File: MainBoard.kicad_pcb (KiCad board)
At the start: 2 copper layers, 95 x 140 mm, 86 parts, among them J1 Conn_01x04, J10 Conn_01x02, J11 Conn_01x03, J12 Conn_01x03, J13 Conn_01x04, J14 Conn_01x03, J15 Conn_01x04, J16 Conn_01x05, J17 Conn_01x05, J18 Conn_01x06, J19 Conn_01x05, J2 Conn_01x04, J20 Conn_01x08, J21 Conn_01x03, J22 Conn_01x03, J23 Conn_01x05, J24 Conn_01x04, J25 Conn_01x04, J26 Conn_01x04, J27 Conn_01x04, J28 Conn_01x04, J3 Conn_01x06, J4 Conn_01x02, J5 Conn_01x02, J6 Conn_01x02, J7 Conn_01x04, J8 Conn_01x04, J9 Conn_01x02, Q1 NMOS_80A, Q10 NMOS_80A, Q11 NMOS_80A, Q2 NMOS_80A, Q3 NMOS_80A, Q4 NMOS, Q5 NMOS, Q6 NMOS, Q7 NMOS, Q8 NMOS, Q9 NMOS, U1 TJA1051T-3, U10 INA228, U2 INA228, U5 INA228, U6 ESP32-DEVKITC-32D, U7 MCP23017_SO, U8 MCP23017_SO, U9 INA228

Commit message: routed a few more track
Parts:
- moved J20 0.79 mm to (100.0, 62.8)
- moved J25 0.49 mm to (108.8, 71.0)
- moved J26 0.24 mm to (109.0, 84.0)
- moved J27 0.24 mm to (109.0, 97.0)
- moved J28 0.16 mm to (109.0, 110.0)
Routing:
- net BRAKE_LEFT_INPUT: track 0.00 -> 132.3 mm, vias 0 -> 3
- net Net-(D6-DOUT): track 0.00 -> 106.3 mm, vias 0 -> 2
- net MAP_INPUT: track 0.00 -> 70.7 mm, vias 0 -> 2
- net MAP_LED: track 0.00 -> 61.6 mm, vias 0 -> 2
- net SDA: track 0.00 -> 44.5 mm, vias 0 -> 2
- net SCL: track 0.00 -> 43.0 mm, vias 0 -> 2
- net +5V: track 64.0 -> 99.6 mm
- net +3.3V: track 66.0 -> 91.2 mm, vias 1 -> 2
- net Net-(J24-Pin_3): track 0.00 -> 3.06 mm
- net CANH: track 249.1 -> 249.8 mm
- net CANL: track 242.4 -> 243.1 mm

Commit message: routing
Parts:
- moved R3 0.75 mm to (89.5, 92.8)
- moved R4 0.50 mm to (89.5, 90.0)
- moved R5 0.25 mm to (89.5, 87.2)
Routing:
- net Net-(D5-DOUT): track 0.00 -> 121.0 mm, vias 0 -> 2
- net POT_SEATDHEATER_X: track 0.00 -> 66.3 mm, vias 0 -> 3
- net POT_SEATHEATER_A: track 0.00 -> 56.9 mm, vias 0 -> 2
- net POT_SEATHEATER_B: track 0.00 -> 55.8 mm
- net TRUNK_LED: track 0.00 -> 55.7 mm, vias 0 -> 2
- net DEFROST_LED: track 0.00 -> 53.5 mm, vias 0 -> 2
- net RGBLED_DIN: track 0.00 -> 50.8 mm, vias 0 -> 1
- net TRUNK_INPUT: track 0.00 -> 48.4 mm, vias 0 -> 1
- net DEFROST_INPUT: track 0.00 -> 35.9 mm
- net PAS_B: track 0.00 -> 25.1 mm, vias 0 -> 1
- net CAN_S: track 3.10 -> 25.0 mm, vias 0 -> 1
- net GND: track 503.6 -> 524.4 mm
- net PAS_A: track 0.00 -> 17.1 mm, vias 0 -> 1
- net +5V: track 99.6 -> 113.9 mm, vias 1 -> 3
- net SDA: track 44.5 -> 55.4 mm
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
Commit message: PCB ready for fab
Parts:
- added G***: LOGO, velion_mainboard:silhouette, B.Cu at (47.8, 67.5)
- R10, R12, R13, R14, R15, R16: value 330 R -> 100 R
- moved R3 52.1 mm to (64.5, 47.0)
- moved R4 47.1 mm to (64.5, 50.0)
- moved R5 42.4 mm to (64.5, 53.0)
- moved C5 6.69 mm to (105.1, 116.5), turned to 180 degrees
- moved J16 0.20 mm to (89.3, 84.0)
- moved U3 0.18 mm to (42.6, 119.9)
- moved U4 0.15 mm to (42.6, 75.0)
- moved J24 0.14 mm to (109.1, 58.0)
- moved J19 0.12 mm to (89.4, 97.0)
- moved J23 0.12 mm to (89.4, 110.0)
- moved R10 0.10 mm to (68.0, 104.0), turned to 0 degrees
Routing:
- net GND: track 524.4 -> 1021.6 mm, vias 2 -> 27
- net +5V: track 113.9 -> 424.0 mm, vias 3 -> 16
- net SDA: track 55.4 -> 312.9 mm, vias 2 -> 12
- net +3.3V: track 97.4 -> 346.1 mm, vias 2 -> 14
- net SCL: track 52.0 -> 297.7 mm, vias 2 -> 12
- net BRAKE_RIGHT_INPUT: track 0.00 -> 134.0 mm, vias 0 -> 4
- net BLINKER_LEFT_MOSFET_GATE: track 0.00 -> 127.4 mm, vias 0 -> 2
- net HANDHEATER_MOSFET_GATE: track 0.00 -> 127.2 mm, vias 0 -> 4
- net POWERINPUT_ALERT: track 0.00 -> 119.7 mm, vias 0 -> 4
- net Net-(D10-DOUT): track 0.00 -> 116.4 mm, vias 0 -> 6
- net Defroster_ALERT: track 0.00 -> 115.3 mm, vias 0 -> 4
- net INTERRIOR_LIGHT_MOSFET_GATE: track 0.00 -> 110.6 mm, vias 0 -> 2
- net SEATHEATER_ALERT: track 0.00 -> 108.7 mm, vias 0 -> 4
- net DRL_LEFT_MOSFET_GATE: track 0.00 -> 107.5 mm, vias 0 -> 5
- net AUXAUDIO_MOSFET_GATE: track 0.00 -> 105.9 mm, vias 0 -> 3
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- added copper zone on B.Cu, net +3.3V
- added copper zone on B.Cu, net VBUS
- added copper zone on B.Cu, net VBUS_CAN_FUSED
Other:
- board text added: "AUDIO"
- board text added: "CAN DISPLAY"
- board text added: "CAN FRONT"
- board text added: "CAN HANDLE"
- board text added: "CAN REAR"
- board text added: "DEFRST BTN"
- board text added: "DFROST"
- board text added: "DIR BTN"
- board text added: "ESP32"
- board text added: "FOG BTN"
- board text added: "FUSE"
- board text added: "HANDLE CABLE"
- board text added: "LEFT BLK"
- board text added: "LIGHT BTN"
- board text added: "Less Mass, More Class"
- board text added: "MAPPING BTN"
- board text added: "MPPT"
- board text added: "Nathann Morand BTF 25"
- board text added: "PAS INPUT"
- board text added: "POT HAND HTER"
- board text added: "POT SEAT HTER"
- board text added: "POT SPEED LMIT"
- board text added: "POWER+CAN IN"
- board text added: "RIGHT BLK"
- board text added: "SEAT CABLE"
- board text added: "THROTTLE"
- board text added: "TRUNK BTN"
- board text added: "TRUNK+LIGHT"
- board text added: "USB C"
- board text added: "USB here"
- board text added: "Velion mainboard v1.0"
- board text added: "WARNING BTN"
- board text added: "antenna here"
- board text added: "eta=Crr*m*g+0.5*rho*Cd*A*v^2"

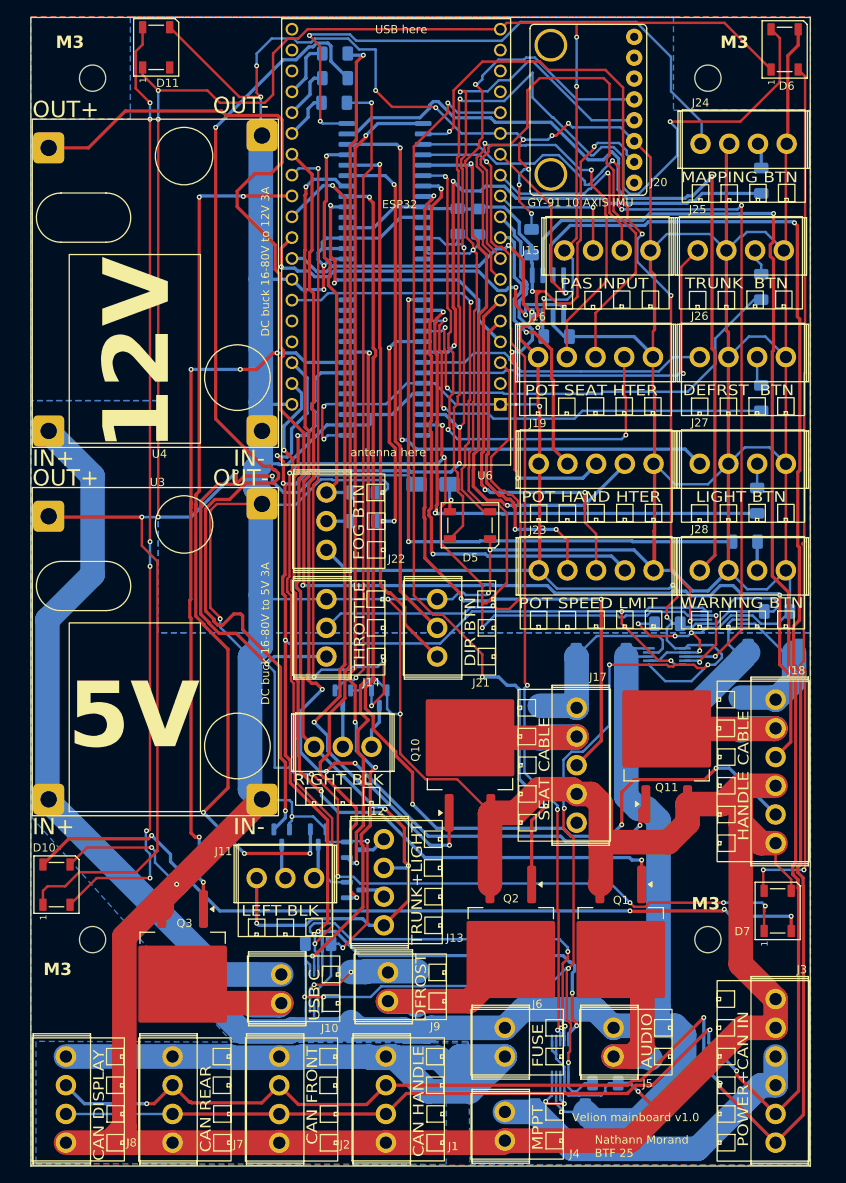
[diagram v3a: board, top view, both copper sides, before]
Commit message: added POWER signal for siliXcon
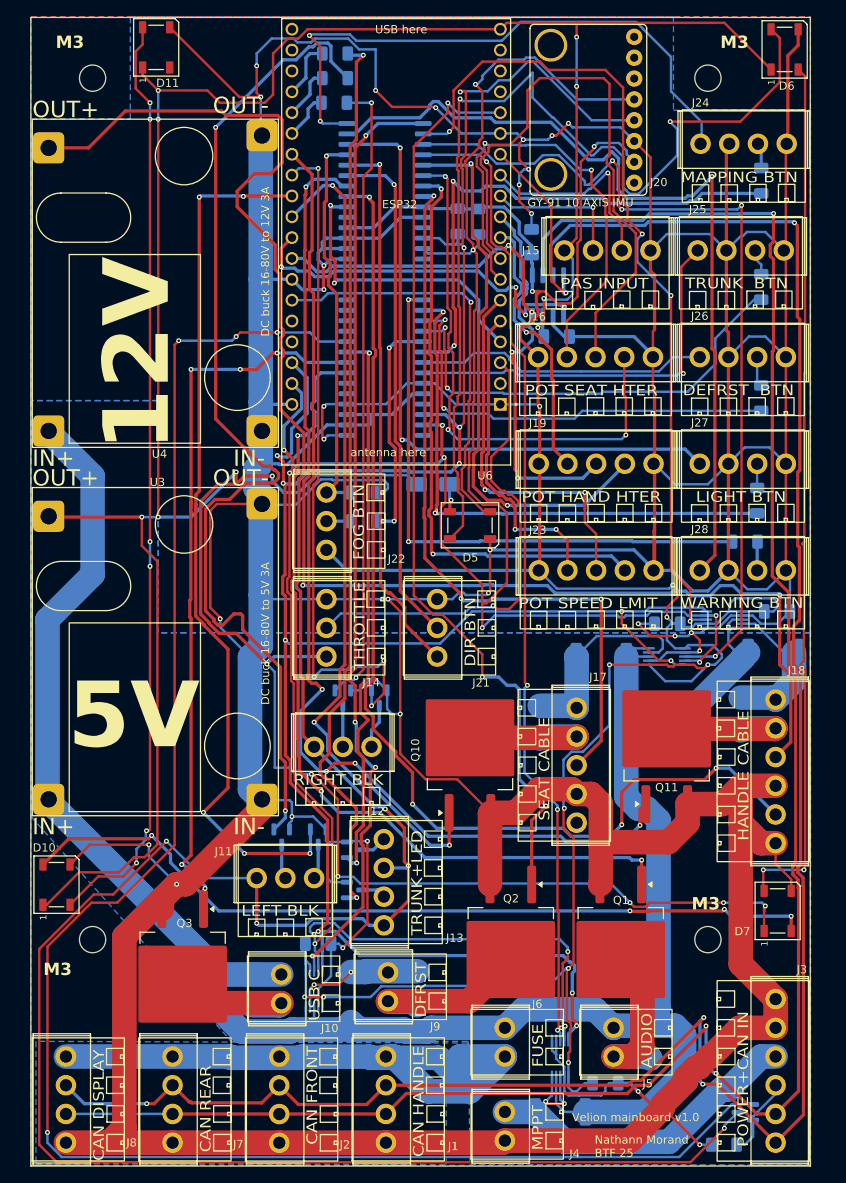
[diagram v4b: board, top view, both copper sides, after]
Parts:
- added Q12: NMOS, Package_TO_SOT_SMD:SOT-23, B.Cu at (114.6, 176.1)
- added R17: 10 K, Resistor_SMD:R_1206_3216Metric_Pad1.30x1.75mm_HandSolder, B.Cu at (112.0, 180.0)
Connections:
- J3 pad 4: Net-(J3-Pin_3) -> POWER
- U7 pad 24: unconnected-(U7-GPA3-Pad24) -> POWER_MOSFET_GATE
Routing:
- net POWER_MOSFET_GATE: track 0.00 -> 217.0 mm, vias 0 -> 4
- net +12V: track 169.0 -> 315.8 mm, vias 3 -> 5
- net POWER: track 0.00 -> 9.80 mm
- net GND: track 1021.6 -> 1030.9 mm, vias 27 -> 28
- net Net-(J3-Pin_3): track 52.6 -> 49.9 mm
- net Net-(D10-DOUT): track 116.4 -> 114.0 mm
- net CANL: track 243.2 -> 245.0 mm
- net +5V: track 424.0 -> 422.5 mm
- net CANH: track 255.4 -> 256.9 mm
- net AUXUSB_MOSFET_GATE: track 87.1 -> 88.1 mm
- net VBUS: track 267.4 -> 266.6 mm
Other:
- board text added: "DFRST"
- board text added: "TRUNK+LED"
- board text removed: "DFROST"
- board text removed: "TRUNK+LIGHT"

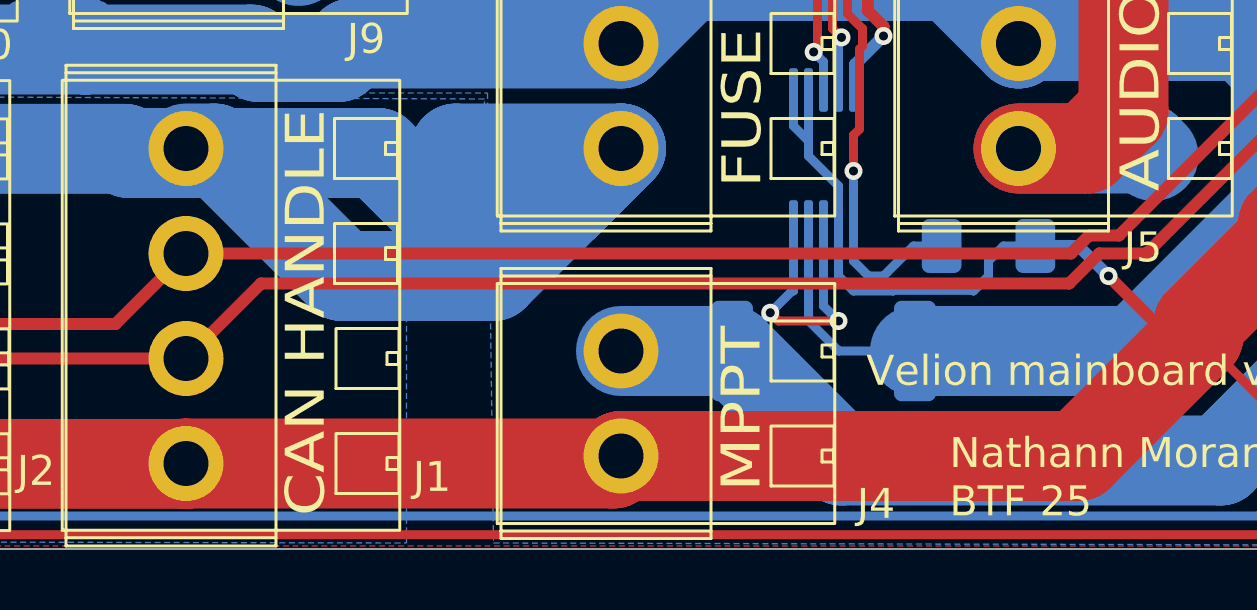
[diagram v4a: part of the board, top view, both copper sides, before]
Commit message: added 120 R CAN terminator
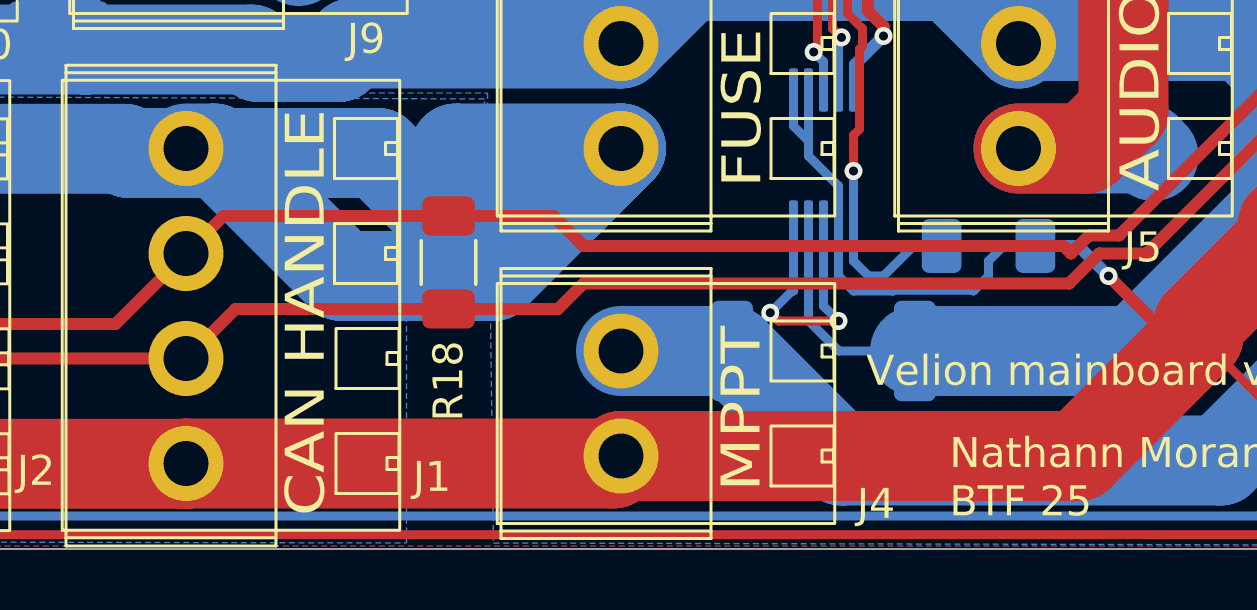
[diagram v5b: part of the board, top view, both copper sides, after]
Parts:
- added R18: 120 R, Resistor_SMD:R_1206_3216Metric_Pad1.30x1.75mm_HandSolder, F.Cu at (79.5, 173.1)
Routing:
- net CANH: track 256.9 -> 257.9 mm
